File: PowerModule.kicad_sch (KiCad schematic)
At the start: 56 parts, among them U20 ADM3485, U21 ADM3485, U22 ADM3485, U23 ADM3485, U24 ADM3485, U25 ADM3485, U26 ADM3485, U66 ADM3485

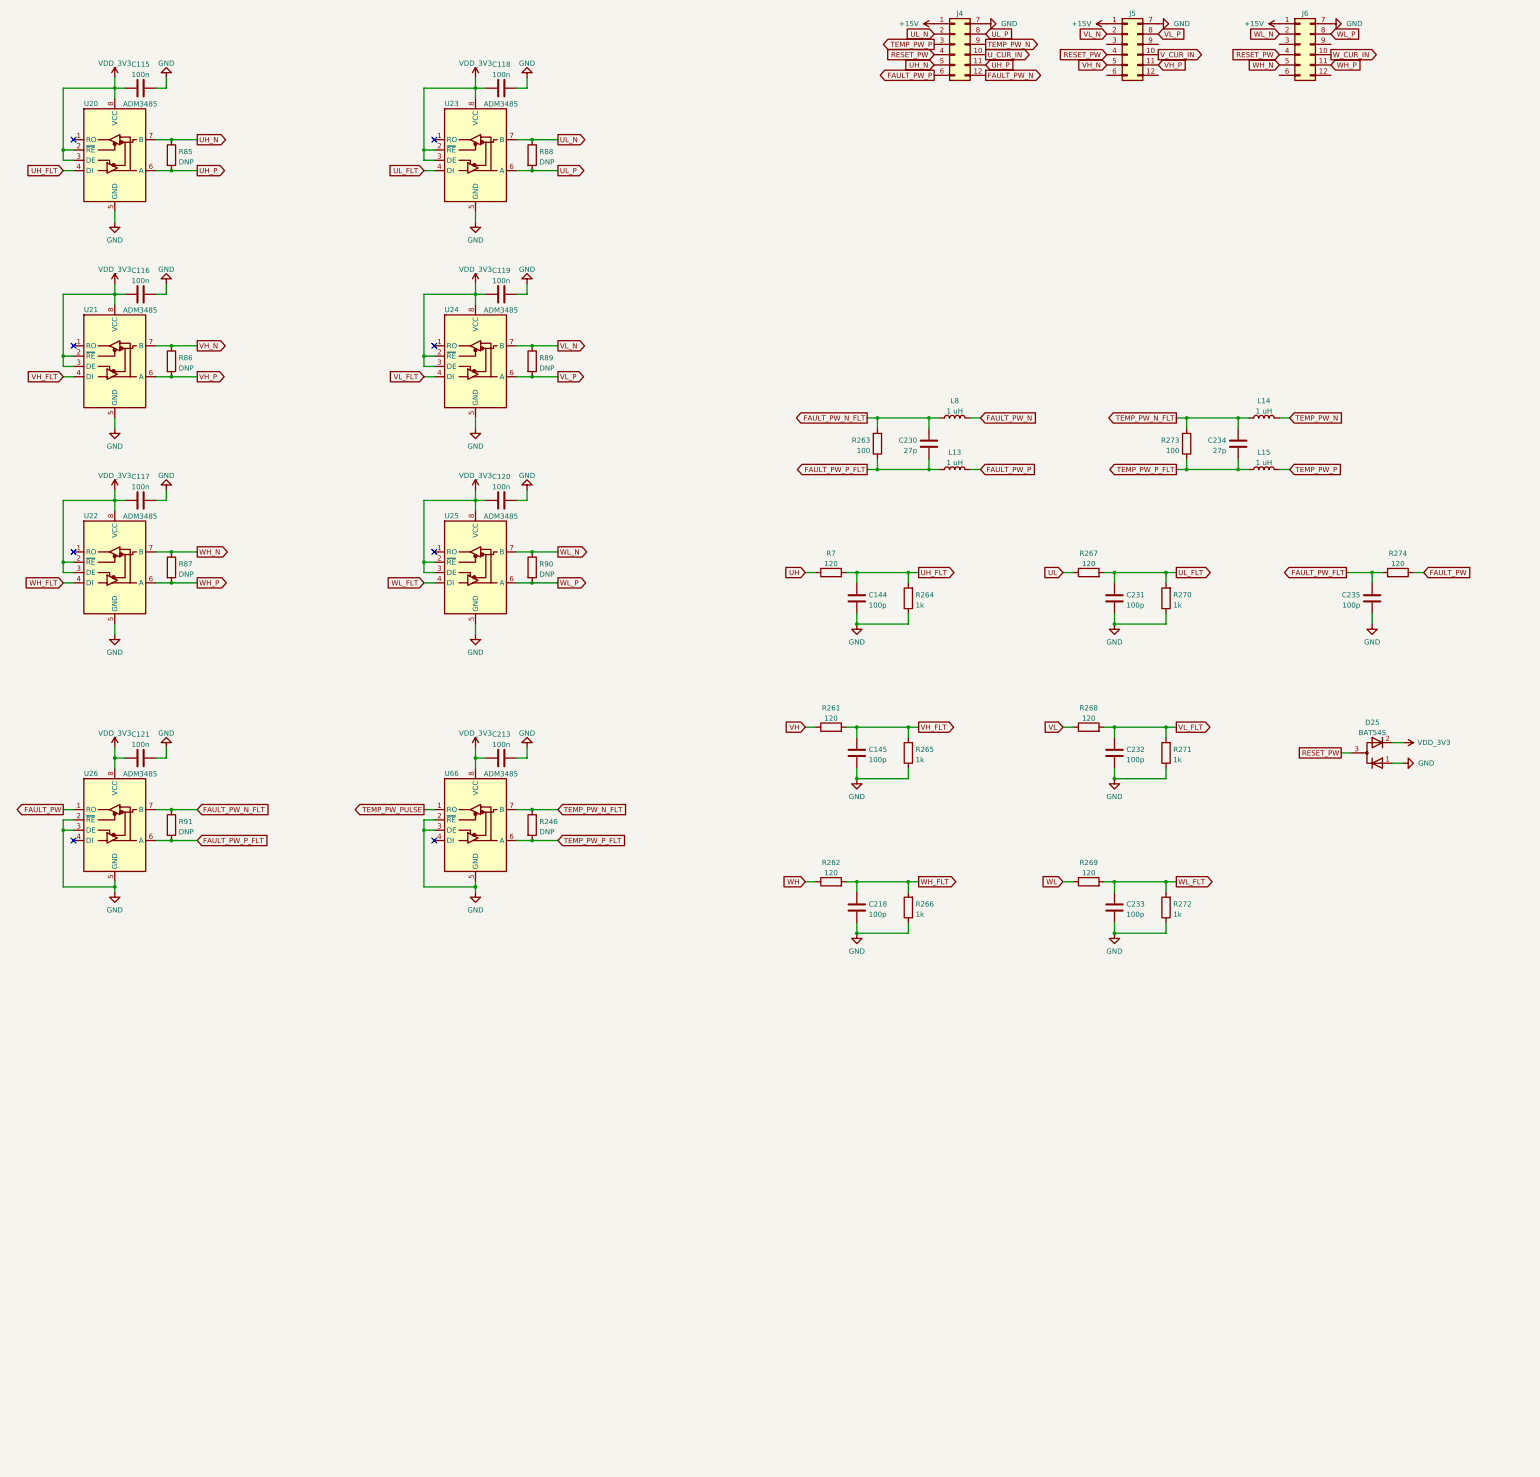
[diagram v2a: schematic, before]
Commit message: Исправление: в схеме добавил обработку температур, изменил обработку токов
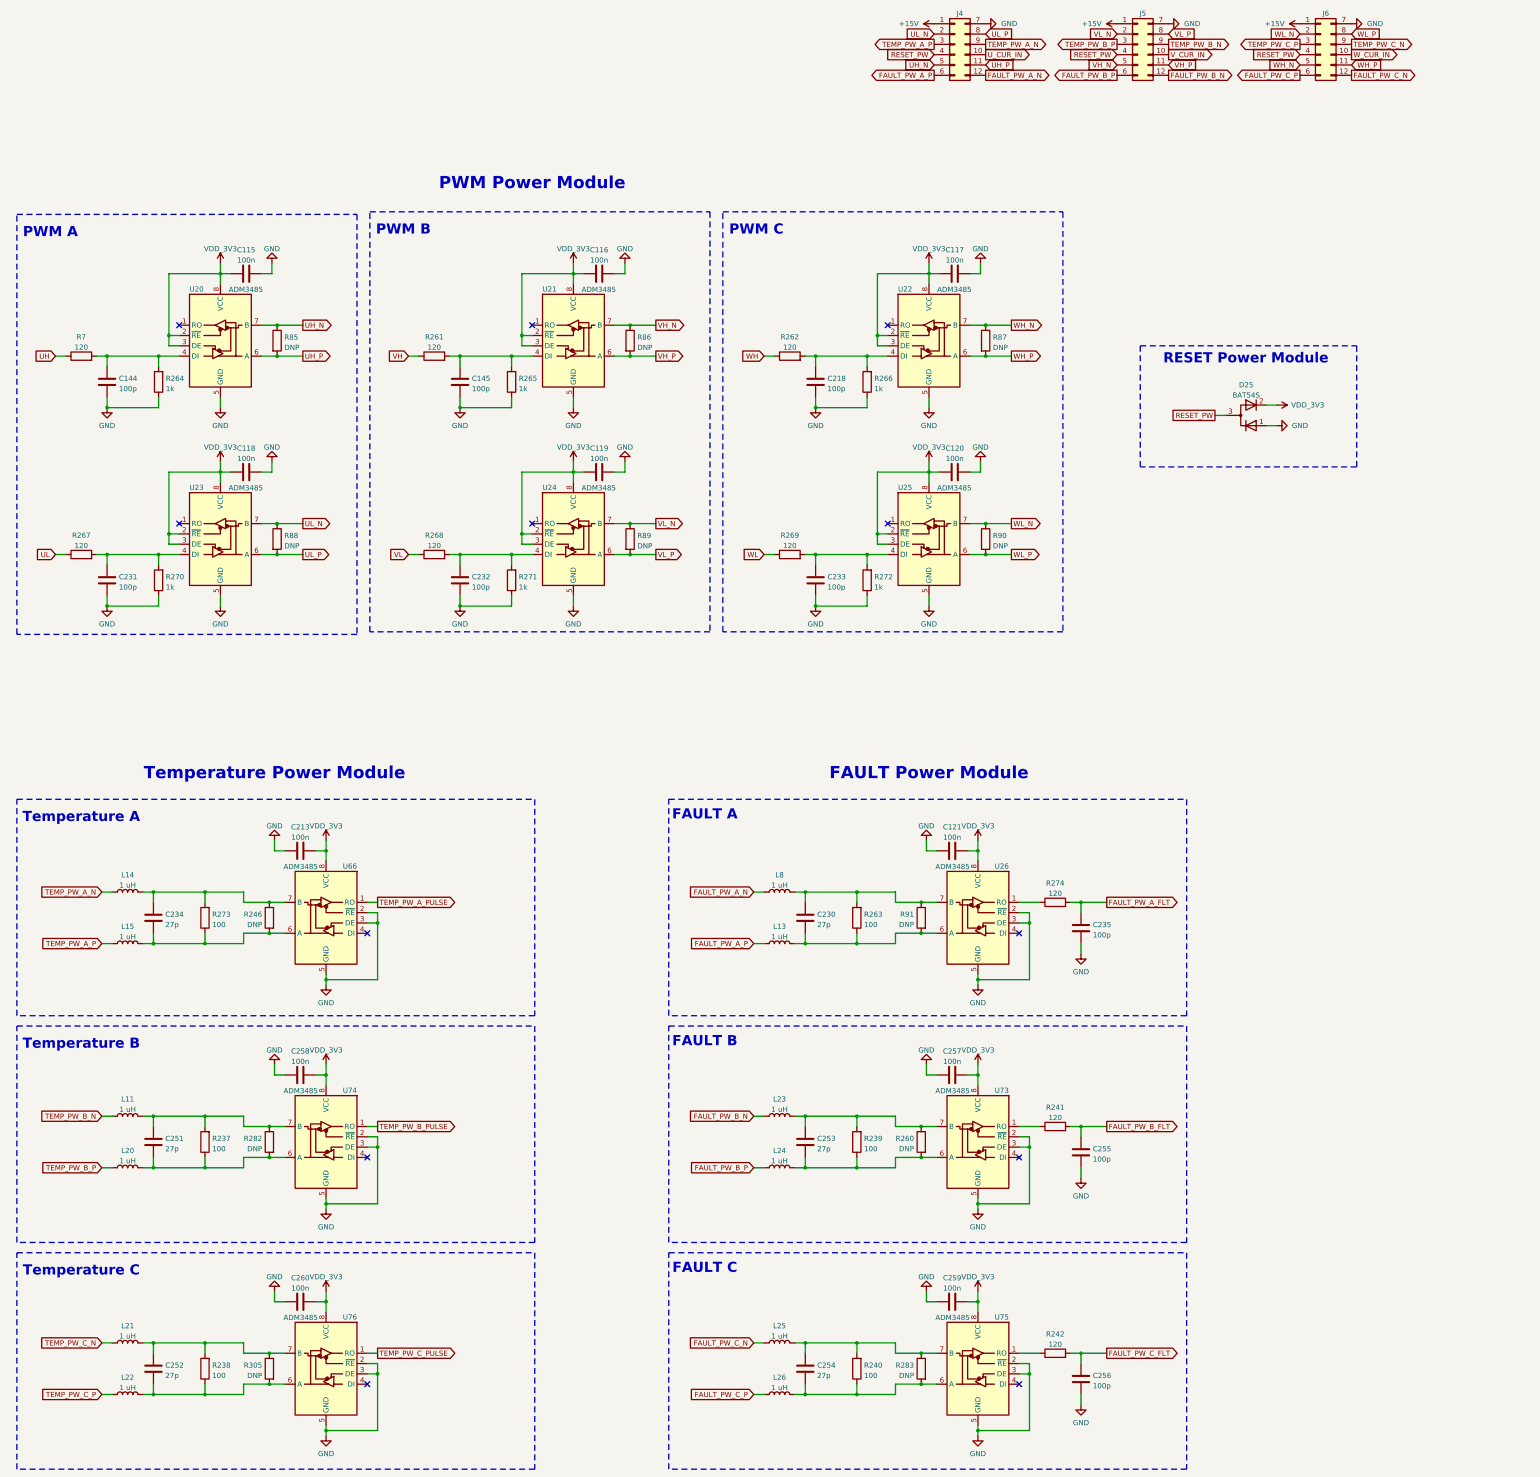
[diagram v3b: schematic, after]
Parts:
- added C251, C252, C253, C254: 27p, Capacitor_SMD:C_0603_1608Metric, symbol Device:C
- added C255, C256: 100p, Capacitor_SMD:C_0603_1608Metric, symbol Device:C
- added C257, C258, C259, C260: 100n, Capacitor_SMD:C_1206_3216Metric, symbol Device:C
- added L11, L20, L21, L22, L23, L24, L25, L26: 1 uH, Inductor_SMD:L_0805_2012Metric, symbol Device:L
- added R237, R238, R239, R240: 100, Resistor_SMD:R_0603_1608Metric, symbol Device:R
- added R241, R242: 120, Resistor_SMD:R_0603_1608Metric, symbol Device:R
- added R260, R282, R283, R305: DNP, Resistor_SMD:R_0805_2012Metric, symbol Device:R
- added U73, U74, U75, U76: ADM3485, Package_SO:SOIC-8_3.9x4.9mm_P1.27mm, symbol Project_Library:ADM3485
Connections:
- net GND: now also C255.2, C256.2, C257.2, C258.2, C259.2, C260.2, U73.2 (~{RE}), U73.3 (DE), U73.5 (GND), U74.2 (~{RE}), U74.3 (DE), U74.5 (GND), U75.2 (~{RE}), U75.3 (DE), U75.5 (GND), U76.2 (~{RE}), U76.3 (DE), U76.5 (GND)
- net VDD_3V3: now also C257.1, C258.1, C259.1, C260.1, U73.8 (VCC), U74.8 (VCC), U75.8 (VCC), U76.8 (VCC)
- net FAULT_PW_C_N: now reaches J6.12 (Pin_12)
- net FAULT_PW_C_N: now also L25.1
- net TEMP_PW_C_P: now reaches J6.3 (Pin_3)
- net TEMP_PW_C_P: now also L22.1
- net FAULT_PW_C_P: now reaches J6.6 (Pin_6)
- net FAULT_PW_C_P: now also L26.1
- net TEMP_PW_C_N: now reaches J6.9 (Pin_9)
- net TEMP_PW_C_N: now also L21.1
- net FAULT_PW_B_N: now reaches J5.12 (Pin_12)
- net FAULT_PW_B_N: now also L23.1
- net TEMP_PW_B_P: now reaches J5.3 (Pin_3)
- net TEMP_PW_B_P: now also L20.1
- net FAULT_PW_B_P: now reaches J5.6 (Pin_6)
- net FAULT_PW_B_P: now also L24.1
- net TEMP_PW_B_N: now reaches J5.9 (Pin_9)
- net TEMP_PW_B_N: now also L11.1
- net FAULT_PW: no longer names the net of R274.1, U26.1 (RO)
- net FAULT_PW_FLT renamed FAULT_PW_A_FLT
- net FAULT_PW_N renamed FAULT_PW_A_N
- net FAULT_PW_N_FLT: no longer names the net of C230.1, L8.2, R263.2, R91.1, U26.7 (B)
- net FAULT_PW_P renamed FAULT_PW_A_P
- net FAULT_PW_P_FLT: no longer names the net of C230.2, L13.2, R263.1, R91.2, U26.6 (A)
- net TEMP_PW_N renamed TEMP_PW_A_N
- net TEMP_PW_N_FLT: no longer names the net of C234.1, L14.2, R246.1, R273.2, U66.7 (B)
- net TEMP_PW_P renamed TEMP_PW_A_P
- net TEMP_PW_PULSE renamed TEMP_PW_A_PULSE
- net TEMP_PW_P_FLT: no longer names the net of C234.2, L15.2, R246.2, R273.1, U66.6 (A)
- net UH_FLT: no longer names the net of C144.1, R264.2, R7.2, U20.4 (DI)
- net UL_FLT: no longer names the net of C231.1, R267.2, R270.2, U23.4 (DI)
- net VH_FLT: no longer names the net of C145.1, R261.2, R265.2, U21.4 (DI)
- net VL_FLT: no longer names the net of C232.1, R268.2, R271.2, U24.4 (DI)
- net WH_FLT: no longer names the net of C218.1, R262.2, R266.2, U22.4 (DI)
- net WL_FLT: no longer names the net of C233.1, R269.2, R272.2, U25.4 (DI)
- new net: C253.1, L23.2, R239.2, R260.1, U73.7 (B)
- new net: C253.2, L24.2, R239.1, R260.2, U73.6 (A)
- new net: C252.2, L22.2, R238.1, R305.2, U76.6 (A)
- new net: R242.1, U75.1 (RO)
- new net: C254.2, L26.2, R240.1, R283.2, U75.6 (A)
- new net: C254.1, L25.2, R240.2, R283.1, U75.7 (B)
- new net: C251.2, L20.2, R237.1, R282.2, U74.6 (A)
- new net: C251.1, L11.2, R237.2, R282.1, U74.7 (B)
- new net: C252.1, L21.2, R238.2, R305.1, U76.7 (B)
- new net: R241.1, U73.1 (RO)
- new net FAULT_PW_B_FLT: C255.1, R241.2
- new net FAULT_PW_C_FLT: C256.1, R242.2
- new net TEMP_PW_B_PULSE: U74.1 (RO)
- new net TEMP_PW_C_PULSE: U76.1 (RO)
- no-connect marks 8 -> 12
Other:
- note added: "FAULT A"
- note added: "FAULT B"
- note added: "FAULT C"
- note added: "FAULT Power Module"
- note added: "PWM A"
- note added: "PWM B"
- note added: "PWM C"
- note added: "PWM Power Module"
- note added: "RESET Power Module"
- note added: "Temperature A"
- note added: "Temperature B"
- note added: "Temperature C"
- note added: "Temperature Power Module"
- moved on the sheet: C115, C116, C117, C118, C119, C120, C121, C144, C145, C213, C218, C230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

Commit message: Изменения: добавил 3или для фолтов трёхфазного модуля
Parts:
- added C241: 100n, Capacitor_SMD:C_0805_2012Metric_Pad1.18x1.45mm_HandSolder, symbol Device:C
- added D3: NC7SZ332P6X, Package_TO_SOT_SMD:SOT-363_SC-70-6_Handsoldering, symbol Project_Library:NC7SZ332P6X
- added R229, R230, R231, R232, R233, R234: 560, Resistor_SMD:R_0603_1608Metric, symbol Device:R
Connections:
- net FAULT_PW_A_FLT: now also D3.1 (A)
- net FAULT_PW_B_FLT: now also D3.3 (B)
- net FAULT_PW_C_FLT: now also D3.6 (C)
- net GND: now also C241.2, D3.2 (GND), R229.2, R232.2, R233.2
- net VDD_3V3: now also C241.1, D3.5 (VCC), R230.1, R231.1, R234.1
- net at C253.1, L23.2, R239.2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: now also R232.1
- net at C253.2, L24.2, R239.1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: now also R231.2
- net at C254.2, L26.2, R240.1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: now also R234.2
- net at C254.1, L25.2, R240.2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: now also R233.1
- net at C230.2, L13.2, R263.1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: now also R230.2
- net at C230.1, L8.2, R263.2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: now also R229.1
- new net FAULT_PW_FLT: D3.4 (Y)

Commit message: Rev C: отправил на проверку в резонит
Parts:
- removed D3: NC7SZ332P6X, Package_TO_SOT_SMD:SOT-363_SC-70-6_Handsoldering, symbol Project_Library:NC7SZ332P6X
- added D3: SN74LVC1G11DBVR, Package_TO_SOT_SMD:SOT-23-6_Handsoldering, symbol Project_Library:SN74LVC1G11DBVR
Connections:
- net FAULT_PW_A_FLT: now also D3.1 (A)
- net FAULT_PW_B_FLT: now also D3.3 (B)
- net FAULT_PW_C_FLT: now also D3.6 (C)
- net FAULT_PW_FLT: now also D3.4 (Y)
- net GND: now also D3.2 (GND)
- net VDD_3V3: now also D3.5 (VCC)
